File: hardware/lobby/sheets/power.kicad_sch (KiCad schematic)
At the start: 4 parts

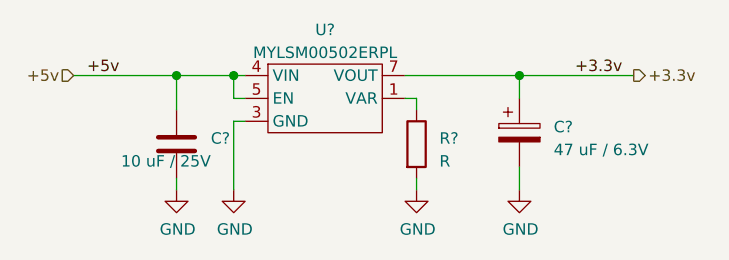
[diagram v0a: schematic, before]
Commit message: start routing mezzanine
making a progress capture before trying to cram a lot of signals onto just one hirose connector...
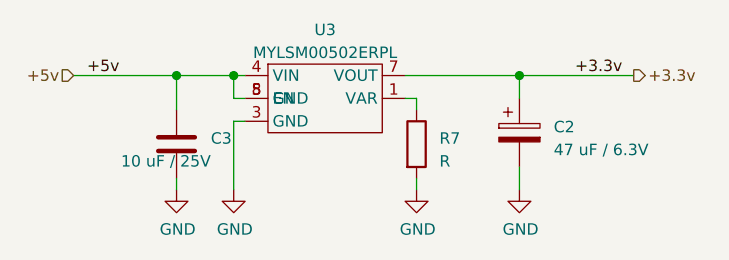
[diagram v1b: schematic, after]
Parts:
- removed U?: MYLSM00502ERPL, CM4IO:MYLSM00502ERPL, symbol CM4IO:MYLSM00502ERPL
- added U3: MYLSM00502ERPL, cm4crypto:MYLSM00502ERPL, symbol cm4crypto:MYLSM00502ERPL
- R7: renamed from R?; footprint (none) -> Resistor_SMD:R_0603_1608Metric
- gave numbers to parts that had none: 2
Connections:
- net +3.3v: now also U3.7 (VOUT)
- net +5v: now also U3.4 (VIN), U3.5 (EN), U3.8 (GND)
- net at R7.1: now also U3.1 (VAR)
- net G-PAD renamed GND
- net GND: now also U3.2 (GND), U3.3 (GND), U3.6 (GND), U3.9 (GND)
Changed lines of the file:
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@@
   (symbol (lib_id "power:GND") (at 127 90.17 0) (unit 1)
     (in_bom yes) (on_board yes)
-    (property "Reference" "#PWR?" (id 0) (at 127 96.52 0)
+    (property "Reference" "#PWR061" (id 0) (at 127 96.52 0)
       (effects (font (size 1.27 1.27)) hide)
     )
@@
   (symbol (lib_id "power:GND") (at 133.35 90.17 0) (unit 1)
     (in_bom yes) (on_board yes)
-    (property "Reference" "#PWR?" (id 0) (at 133.35 96.52 0)
+    (property "Reference" "#PWR062" (id 0) (at 133.35 96.52 0)
       (effects (font (size 1.27 1.27)) hide)
     )
@@
   (symbol (lib_id "power:GND") (at 153.67 90.17 0) (unit 1)
     (in_bom yes) (on_board yes)
-    (property "Reference" "#PWR?" (id 0) (at 153.67 96.52 0)
+    (property "Reference" "#PWR063" (id 0) (at 153.67 96.52 0)
       (effects (font (size 1.27 1.27)) hide)
     )
@@
   (symbol (lib_id "power:GND") (at 165.1 90.17 0) (unit 1)
     (in_bom yes) (on_board yes)
-    (property "Reference" "#PWR?" (id 0) (at 165.1 96.52 0)
+    (property "Reference" "#PWR064" (id 0) (at 165.1 96.52 0)
       (effects (font (size 1.27 1.27)) hide)
     )
@@
   (symbol (lib_id "Device:R") (at 153.67 85.09 0) (unit 1)
     (in_bom yes) (on_board yes) (fields_autoplaced)
-    (property "Reference" "R?" (id 0) (at 156.21 84.4549 0)
+    (property "Reference" "R7" (id 0) (at 156.21 84.4549 0)
       (effects (font (size 1.27 1.27)) (justify left))
     )
@@
       (effects (font (size 1.27 1.27)) (justify left))
     )
-    (property "Footprint" "" (id 2) (at 151.892 85.09 90)
+    (property "Footprint" "Resistor_SMD:R_0603_1608Metric" (id 2) (at 151.892 85.09 90)
       (effects (font (size 1.27 1.27)) hide)
     )
@@
   (symbol (lib_id "Device:C") (at 127 85.09 0) (unit 1)
     (in_bom yes) (on_board yes) (fields_autoplaced)
-    (property "Reference" "C?" (id 0) (at 130.81 84.4549 0)
+    (property "Reference" "C3" (id 0) (at 130.81 84.4549 0)
       (effects (font (size 1.27 1.27)) (justify left))
     )
@@
   (symbol (lib_id "Device:C_Polarized") (at 165.1 83.82 0) (unit 1)
     (in_bom yes) (on_board yes) (fields_autoplaced)
-    (property "Reference" "C?" (id 0) (at 168.91 83.1849 0)
+    (property "Reference" "C2" (id 0) (at 168.91 83.1849 0)
       (effects (font (size 1.27 1.27)) (justify left))
     )
@@
     (pin "2")
   )
-  (symbol (lib_id "CM4IO:MYLSM00502ERPL") (at 143.51 80.01 0) (unit 1)
+  (symbol (lib_id "cm4crypto:MYLSM00502ERPL") (at 143.51 80.01 0) (unit 1)
     (in_bom yes) (on_board yes) (fields_autoplaced)
-    (property "Reference" "U?" (id 0) (at 143.51 72.39 0))
+    (property "Reference" "U3" (id 0) (at 143.51 72.39 0))
     (property "Value" "MYLSM00502ERPL" (id 1) (at 143.51 74.93 0))
-    (property "Footprint" "CM4IO:MYLSM00502ERPL" (id 2) (at 143.51 86.36 0)
+    (property "Footprint" "cm4crypto:MYLSM00502ERPL" (id 2) (at 143.51 86.36 0)
       (effects (font (size 1.27 1.27)) hide)
     )
@@
     (pin "6")
     (pin "7")
+    (pin "8")
     (pin "9")
     (pin "4")

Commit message: sheet refs relative, copied escalator pinout to lobby
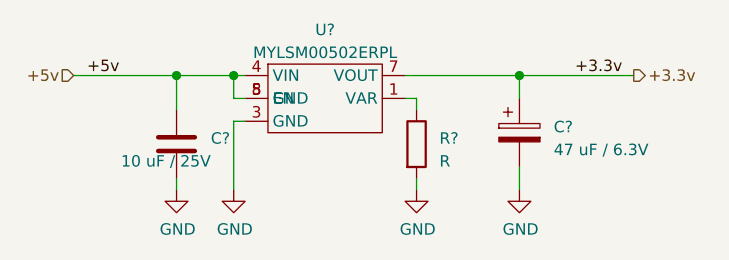
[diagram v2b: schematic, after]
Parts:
- renumbered C2 to C?, C3 to C?, R7 to R?, U3 to U?
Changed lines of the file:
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@@
   (symbol (lib_id "power:GND") (at 127 90.17 0) (unit 1)
     (in_bom yes) (on_board yes)
-    (property "Reference" "#PWR061" (id 0) (at 127 96.52 0)
+    (property "Reference" "#PWR?" (id 0) (at 127 96.52 0)
       (effects (font (size 1.27 1.27)) hide)
     )
@@
   (symbol (lib_id "power:GND") (at 133.35 90.17 0) (unit 1)
     (in_bom yes) (on_board yes)
-    (property "Reference" "#PWR062" (id 0) (at 133.35 96.52 0)
+    (property "Reference" "#PWR?" (id 0) (at 133.35 96.52 0)
       (effects (font (size 1.27 1.27)) hide)
     )
@@
   (symbol (lib_id "power:GND") (at 153.67 90.17 0) (unit 1)
     (in_bom yes) (on_board yes)
-    (property "Reference" "#PWR063" (id 0) (at 153.67 96.52 0)
+    (property "Reference" "#PWR?" (id 0) (at 153.67 96.52 0)
       (effects (font (size 1.27 1.27)) hide)
     )
@@
   (symbol (lib_id "power:GND") (at 165.1 90.17 0) (unit 1)
     (in_bom yes) (on_board yes)
-    (property "Reference" "#PWR064" (id 0) (at 165.1 96.52 0)
+    (property "Reference" "#PWR?" (id 0) (at 165.1 96.52 0)
       (effects (font (size 1.27 1.27)) hide)
     )
@@
   (symbol (lib_id "Device:R") (at 153.67 85.09 0) (unit 1)
     (in_bom yes) (on_board yes) (fields_autoplaced)
-    (property "Reference" "R7" (id 0) (at 156.21 84.4549 0)
+    (property "Reference" "R?" (id 0) (at 156.21 84.4549 0)
       (effects (font (size 1.27 1.27)) (justify left))
     )
@@
   (symbol (lib_id "Device:C") (at 127 85.09 0) (unit 1)
     (in_bom yes) (on_board yes) (fields_autoplaced)
-    (property "Reference" "C3" (id 0) (at 130.81 84.4549 0)
+    (property "Reference" "C?" (id 0) (at 130.81 84.4549 0)
       (effects (font (size 1.27 1.27)) (justify left))
     )
@@
   (symbol (lib_id "Device:C_Polarized") (at 165.1 83.82 0) (unit 1)
     (in_bom yes) (on_board yes) (fields_autoplaced)
-    (property "Reference" "C2" (id 0) (at 168.91 83.1849 0)
+    (property "Reference" "C?" (id 0) (at 168.91 83.1849 0)
       (effects (font (size 1.27 1.27)) (justify left))
     )
@@
   (symbol (lib_id "cm4crypto:MYLSM00502ERPL") (at 143.51 80.01 0) (unit 1)
     (in_bom yes) (on_board yes) (fields_autoplaced)
-    (property "Reference" "U3" (id 0) (at 143.51 72.39 0))
+    (property "Reference" "U?" (id 0) (at 143.51 72.39 0))
     (property "Value" "MYLSM00502ERPL" (id 1) (at 143.51 74.93 0))
     (property "Footprint" "cm4crypto:MYLSM00502ERPL" (id 2) (at 143.51 86.36 0)

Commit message: work abroad
did some light planning for the lobby board while on vacation. now ready for final placement + routing
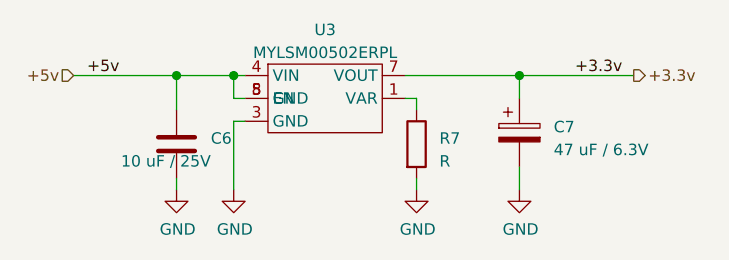
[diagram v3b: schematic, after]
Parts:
- C6: renamed from C?; footprint Capacitor_SMD:C_0805_2012Metric -> Capacitor_SMD:C_0603_1608Metric
- gave numbers to parts that had none: 3
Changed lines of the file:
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@@
   (symbol (lib_id "power:GND") (at 127 90.17 0) (unit 1)
     (in_bom yes) (on_board yes)
-    (property "Reference" "#PWR?" (id 0) (at 127 96.52 0)
+    (property "Reference" "#PWR065" (id 0) (at 127 96.52 0)
       (effects (font (size 1.27 1.27)) hide)
     )
@@
   (symbol (lib_id "power:GND") (at 133.35 90.17 0) (unit 1)
     (in_bom yes) (on_board yes)
-    (property "Reference" "#PWR?" (id 0) (at 133.35 96.52 0)
+    (property "Reference" "#PWR066" (id 0) (at 133.35 96.52 0)
       (effects (font (size 1.27 1.27)) hide)
     )
@@
   (symbol (lib_id "power:GND") (at 153.67 90.17 0) (unit 1)
     (in_bom yes) (on_board yes)
-    (property "Reference" "#PWR?" (id 0) (at 153.67 96.52 0)
+    (property "Reference" "#PWR067" (id 0) (at 153.67 96.52 0)
       (effects (font (size 1.27 1.27)) hide)
     )
@@
   (symbol (lib_id "power:GND") (at 165.1 90.17 0) (unit 1)
     (in_bom yes) (on_board yes)
-    (property "Reference" "#PWR?" (id 0) (at 165.1 96.52 0)
+    (property "Reference" "#PWR068" (id 0) (at 165.1 96.52 0)
       (effects (font (size 1.27 1.27)) hide)
     )
@@
   (symbol (lib_id "Device:R") (at 153.67 85.09 0) (unit 1)
     (in_bom yes) (on_board yes) (fields_autoplaced)
-    (property "Reference" "R?" (id 0) (at 156.21 84.4549 0)
+    (property "Reference" "R7" (id 0) (at 156.21 84.4549 0)
       (effects (font (size 1.27 1.27)) (justify left))
     )
@@
   (symbol (lib_id "Device:C") (at 127 85.09 0) (unit 1)
     (in_bom yes) (on_board yes) (fields_autoplaced)
-    (property "Reference" "C?" (id 0) (at 130.81 84.4549 0)
+    (property "Reference" "C6" (id 0) (at 130.81 84.4549 0)
       (effects (font (size 1.27 1.27)) (justify left))
     )
@@
       (effects (font (size 1.27 1.27)) (justify right))
     )
-    (property "Footprint" "Capacitor_SMD:C_0805_2012Metric" (id 2) (at 127.9652 88.9 0)
+    (property "Footprint" "Capacitor_SMD:C_0603_1608Metric" (id 2) (at 127.9652 88.9 0)
       (effects (font (size 1.27 1.27)) hide)
     )
@@
   (symbol (lib_id "Device:C_Polarized") (at 165.1 83.82 0) (unit 1)
     (in_bom yes) (on_board yes) (fields_autoplaced)
-    (property "Reference" "C?" (id 0) (at 168.91 83.1849 0)
+    (property "Reference" "C7" (id 0) (at 168.91 83.1849 0)
       (effects (font (size 1.27 1.27)) (justify left))
     )
@@
   (symbol (lib_id "cm4crypto:MYLSM00502ERPL") (at 143.51 80.01 0) (unit 1)
     (in_bom yes) (on_board yes) (fields_autoplaced)
-    (property "Reference" "U?" (id 0) (at 143.51 72.39 0))
+    (property "Reference" "U3" (id 0) (at 143.51 72.39 0))
     (property "Value" "MYLSM00502ERPL" (id 1) (at 143.51 74.93 0))
     (property "Footprint" "cm4crypto:MYLSM00502ERPL" (id 2) (at 143.51 86.36 0)

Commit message: place lobby components
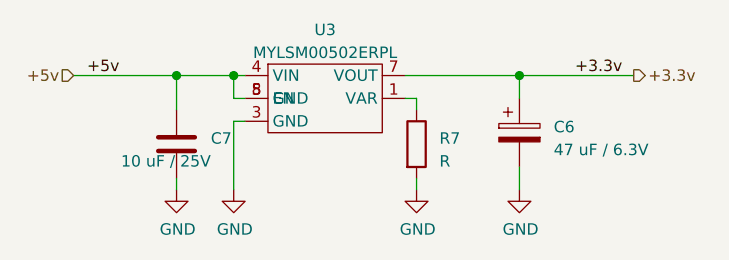
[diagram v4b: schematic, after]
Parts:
- renumbered C7 to C6, C6 to C7
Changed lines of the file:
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@@
   (symbol (lib_id "Device:C") (at 127 85.09 0) (unit 1)
     (in_bom yes) (on_board yes) (fields_autoplaced)
-    (property "Reference" "C6" (id 0) (at 130.81 84.4549 0)
+    (property "Reference" "C7" (id 0) (at 130.81 84.4549 0)
       (effects (font (size 1.27 1.27)) (justify left))
     )
@@
   (symbol (lib_id "Device:C_Polarized") (at 165.1 83.82 0) (unit 1)
     (in_bom yes) (on_board yes) (fields_autoplaced)
-    (property "Reference" "C7" (id 0) (at 168.91 83.1849 0)
+    (property "Reference" "C6" (id 0) (at 168.91 83.1849 0)
       (effects (font (size 1.27 1.27)) (justify left))
     )

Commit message: update lobby
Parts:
- renumbered R7 to R9
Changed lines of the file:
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@@
   (symbol (lib_id "power:GND") (at 127 90.17 0) (unit 1)
     (in_bom yes) (on_board yes)
-    (property "Reference" "#PWR065" (id 0) (at 127 96.52 0)
+    (property "Reference" "#PWR064" (id 0) (at 127 96.52 0)
       (effects (font (size 1.27 1.27)) hide)
     )
@@
   (symbol (lib_id "power:GND") (at 133.35 90.17 0) (unit 1)
     (in_bom yes) (on_board yes)
-    (property "Reference" "#PWR066" (id 0) (at 133.35 96.52 0)
+    (property "Reference" "#PWR065" (id 0) (at 133.35 96.52 0)
       (effects (font (size 1.27 1.27)) hide)
     )
@@
   (symbol (lib_id "power:GND") (at 153.67 90.17 0) (unit 1)
     (in_bom yes) (on_board yes)
-    (property "Reference" "#PWR067" (id 0) (at 153.67 96.52 0)
+    (property "Reference" "#PWR066" (id 0) (at 153.67 96.52 0)
       (effects (font (size 1.27 1.27)) hide)
     )
@@
   (symbol (lib_id "power:GND") (at 165.1 90.17 0) (unit 1)
     (in_bom yes) (on_board yes)
-    (property "Reference" "#PWR068" (id 0) (at 165.1 96.52 0)
+    (property "Reference" "#PWR067" (id 0) (at 165.1 96.52 0)
       (effects (font (size 1.27 1.27)) hide)
     )
@@
   (symbol (lib_id "Device:R") (at 153.67 85.09 0) (unit 1)
     (in_bom yes) (on_board yes) (fields_autoplaced)
-    (property "Reference" "R7" (id 0) (at 156.21 84.4549 0)
+    (property "Reference" "R9" (id 0) (at 156.21 84.4549 0)
       (effects (font (size 1.27 1.27)) (justify left))
     )

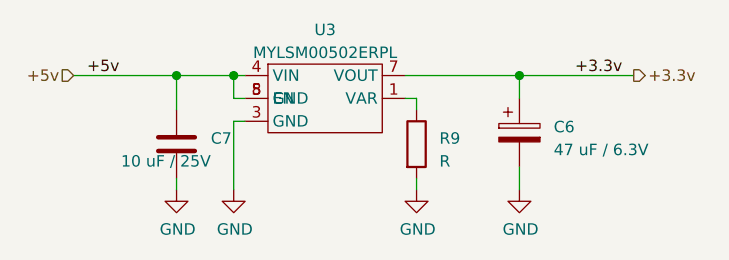
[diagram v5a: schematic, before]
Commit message: mirror lobby mezzanine connector
fixing a big whoops
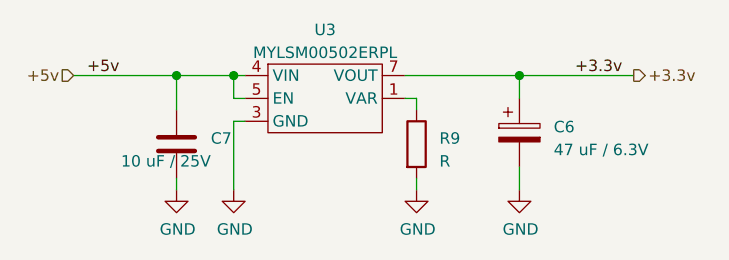
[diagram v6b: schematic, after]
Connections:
- net +5v: no longer U3.8 (GND)
- net GND: now also U3.8 (GND)

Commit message: modify footprints
add paste on hdmi and usbc
add silkscreen outline on murata dcdc supply
change PS cap footprint to polarized footprint
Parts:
- C6: footprint Capacitor_SMD:C_0805_2012Metric -> Capacitor_Tantalum_SMD:CP_EIA-2012-15_AVX-P
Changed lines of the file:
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@@
       (effects (font (size 1.27 1.27)) (justify left))
     )
-    (property "Footprint" "Capacitor_SMD:C_0805_2012Metric" (id 2) (at 166.0652 87.63 0)
+    (property "Footprint" "Capacitor_Tantalum_SMD:CP_EIA-2012-15_AVX-P" (id 2) (at 166.0652 87.63 0)
       (effects (font (size 1.27 1.27)) hide)
     )
